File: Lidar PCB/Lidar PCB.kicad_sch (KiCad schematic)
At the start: 44 parts, among them J1 Barrel_Jack, J2 USB_C_Receptacle_USB2.0, J3 Conn_01x02_Socket, J4 Conn_01x06_Pin, J5 Conn_01x06_Socket, Q1 IRF740, SW1 SW_Push, U1 AMS1117-5.0, U2 ATmega328P-A, U3 FT232RL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

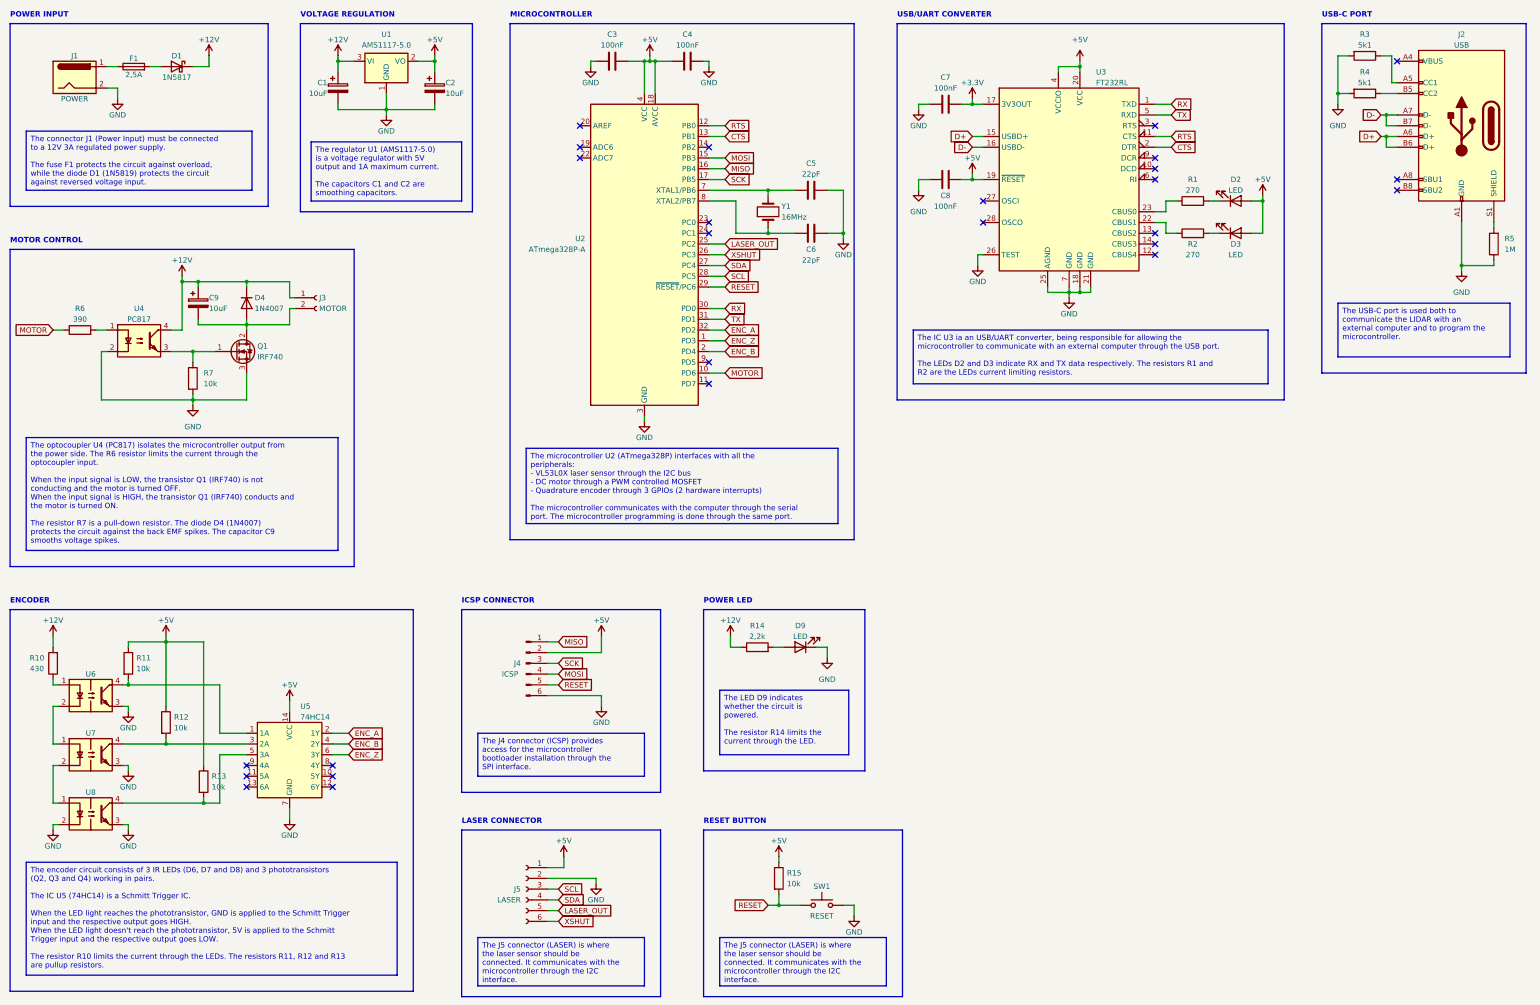
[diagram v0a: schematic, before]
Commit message: PCB input diode removed
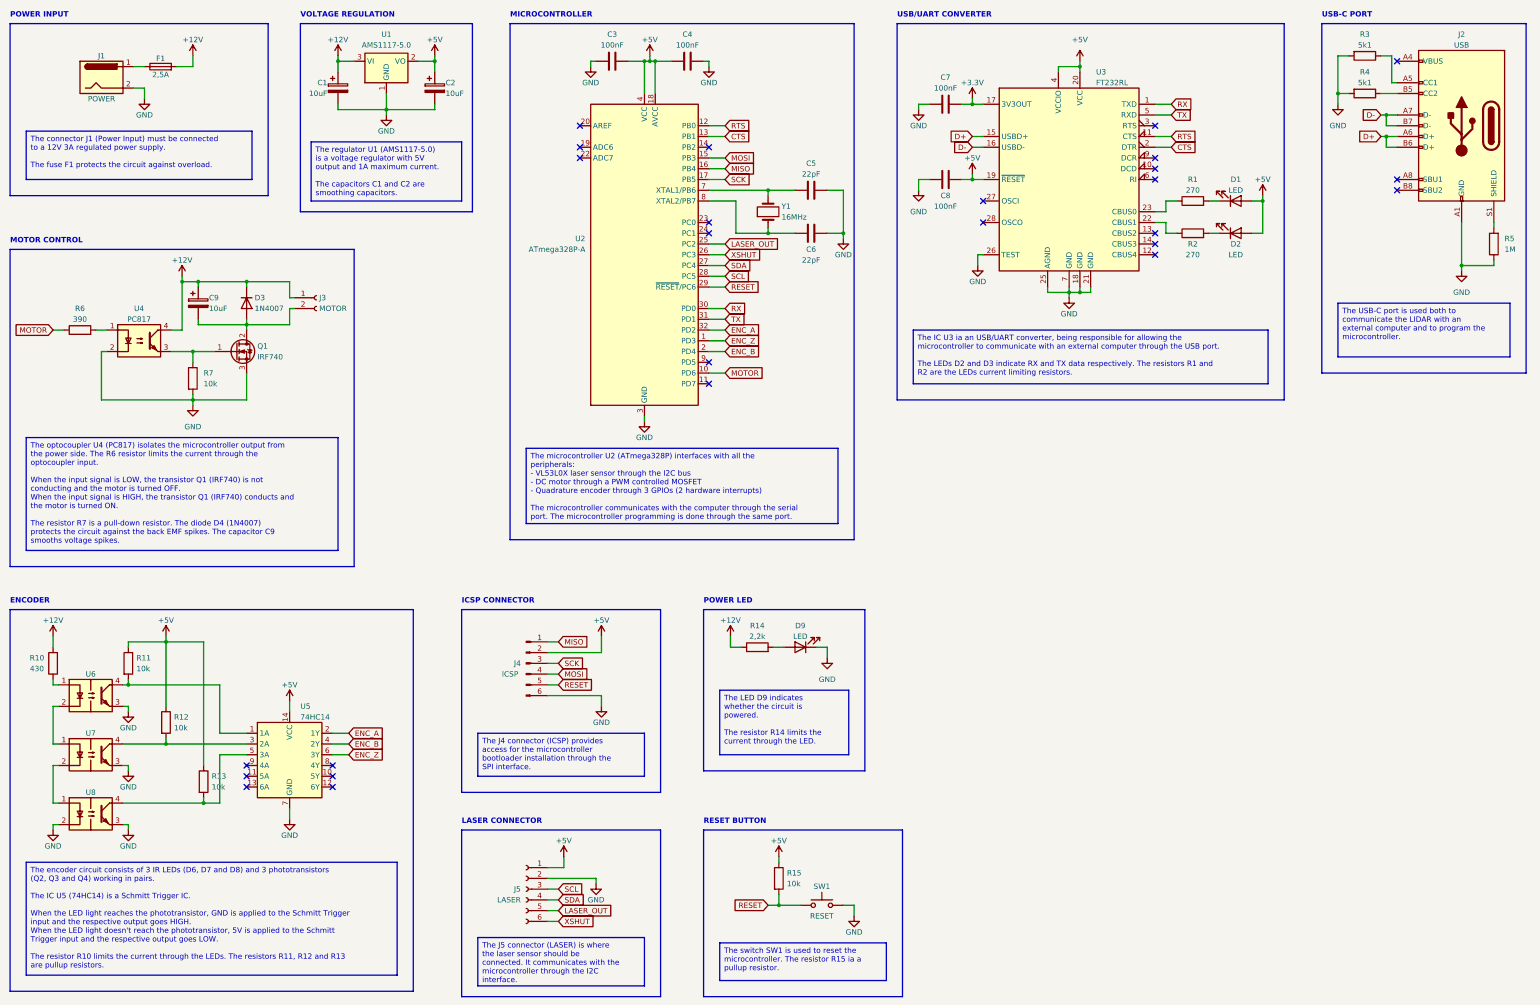
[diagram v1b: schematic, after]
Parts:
- removed D1: 1N5817, Diode_SMD:D_SMA, symbol Diode:1N5819
- renumbered D2 to D1, D3 to D2, D4 to D3
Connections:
- net +12V: now also F1.2
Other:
- moved on the sheet: F1, J1
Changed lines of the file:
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@@
     (stroke (width 0) (type default))
   )
-  (wire (pts (xy 72.39 41.91) (xy 76.2 41.91))
-    (stroke (width 0) (type default))
-  )
   (wire (pts (xy 78.74 204.47) (xy 85.09 204.47))
     (stroke (width 0) (type default))
@@
     (stroke (width 0) (type default))
   )
-  (wire (pts (xy 312.42 73.66) (xy 314.96 73.66))
-    (stroke (width 0) (type default))
-  )
   (wire (pts (xy 279.4 95.25) (xy 279.4 96.52))
     (stroke (width 0) (type default))
@@
     (stroke (width 0) (type default))
   )
-  (wire (pts (xy 76.2 41.91) (xy 76.2 39.37))
+  (wire (pts (xy 72.39 41.91) (xy 72.39 39.37))
     (stroke (width 0) (type default))
   )
@@
     (stroke (width 0) (type default))
   )
-  (wire (pts (xy 52.07 46.99) (xy 54.61 46.99))
+  (wire (pts (xy 58.42 46.99) (xy 60.96 46.99))
     (stroke (width 0) (type default))
   )
-  (wire (pts (xy 54.61 46.99) (xy 54.61 49.53))
+  (wire (pts (xy 60.96 46.99) (xy 60.96 49.53))
     (stroke (width 0) (type default))
   )
@@
     (stroke (width 0) (type default))
   )
+  (wire (pts (xy 312.42 73.66) (xy 314.96 73.66))
+    (stroke (width 0) (type default))
+  )
   (wire (pts (xy 353.06 39.37) (xy 355.6 39.37))
     (stroke (width 0) (type default))
@@
     (stroke (width 0) (type default))
   )
-  (wire (pts (xy 62.23 41.91) (xy 64.77 41.91))
+  (wire (pts (xy 68.58 41.91) (xy 72.39 41.91))
     (stroke (width 0) (type default))
   )
@@
     (stroke (width 0) (type default))
   )
-  (wire (pts (xy 52.07 41.91) (xy 54.61 41.91))
+  (wire (pts (xy 58.42 41.91) (xy 60.96 41.91))
     (stroke (width 0) (type default))
   )
@@
     (fill (type none))
   )
-  (rectangle (start 29.21 31.75) (end 90.17 74.93)
+  (rectangle (start 29.21 31.75) (end 90.17 72.39)
     (stroke (width 0) (type default))
     (fill (type none))
@@
     (effects (font (size 1.27 1.27)) (justify left top))
   )
-  (text_box "The connector J1 (Power Input) must be connected to a 12V 3A regulated power supply.\n\nThe fuse F1 protects the circuit against overload, while the diode D1 (1N5819) protects the circuit against reversed voltage input."
-    (at 33.02 57.15 0) (size 53.34 13.97)
+  (text_box "The connector J1 (Power Input) must be connected to a 12V 3A regulated power supply.\n\nThe fuse F1 protects the circuit against overload."
+    (at 33.02 57.15 0) (size 53.34 11.43)
     (stroke (width 0.3) (type default))
     (fill (type color) (color 194 194 194 1))
@@
     (effects (font (size 1.27 1.27)) (justify left top))
   )
-  (text_box "The J5 connector (LASER) is where the laser sensor should be connected. It communicates with the microcontroller through the I2C interface."
-    (at 196.85 247.65 0) (size 39.37 11.43)
+  (text_box "The switch SW1 is used to reset the microcontroller. The resistor R15 ia a pullup resistor."
+    (at 196.85 248.92 0) (size 39.37 8.89)
     (stroke (width 0.3) (type default))
     (fill (type color) (color 194 194 194 1))
@@
     )
   )
-  (symbol (lib_id "power:+12V") (at 76.2 39.37 0) (unit 1)
+  (symbol (lib_id "power:+12V") (at 72.39 39.37 0) (unit 1)
     (in_bom yes) (on_board yes) (dnp no)
-    (property "Reference" "#PWR02" (at 76.2 43.18 0)
+    (property "Reference" "#PWR02" (at 72.39 43.18 0)
       (effects (font (size 1.27 1.27)) hide)
     )
-    (property "Value" "+12V" (at 76.2 35.56 0)
+    (property "Value" "+12V" (at 72.39 35.56 0)
       (effects (font (size 1.27 1.27)))
     )
-    (property "Footprint" "" (at 76.2 39.37 0)
+    (property "Footprint" "" (at 72.39 39.37 0)
       (effects (font (size 1.27 1.27)) hide)
     )
-    (property "Datasheet" "" (at 76.2 39.37 0)
+    (property "Datasheet" "" (at 72.39 39.37 0)
       (effects (font (size 1.27 1.27)) hide)
     )
@@
     )
   )
-  (symbol (lib_id "power:GND") (at 54.61 49.53 0) (unit 1)
+  (symbol (lib_id "power:GND") (at 60.96 49.53 0) (unit 1)
     (in_bom yes) (on_board yes) (dnp no)
-    (property "Reference" "#PWR01" (at 54.61 55.88 0)
+    (property "Reference" "#PWR01" (at 60.96 55.88 0)
       (effects (font (size 1.27 1.27)) hide)
     )
-    (property "Value" "GND" (at 54.61 53.34 0)
+    (property "Value" "GND" (at 60.96 53.34 0)
       (effects (font (size 1.27 1.27)))
     )
-    (property "Footprint" "" (at 54.61 49.53 0)
+    (property "Footprint" "" (at 60.96 49.53 0)
       (effects (font (size 1.27 1.27)) hide)
     )
-    (property "Datasheet" "" (at 54.61 49.53 0)
+    (property "Datasheet" "" (at 60.96 49.53 0)
       (effects (font (size 1.27 1.27)) hide)
     )
@@
   (symbol (lib_id "Device:LED") (at 318.77 73.66 0) (mirror x) (unit 1)
     (in_bom yes) (on_board yes) (dnp no)
-    (property "Reference" "D2" (at 318.77 68.58 0)
+    (property "Reference" "D1" (at 318.77 68.58 0)
       (effects (font (size 1.27 1.27)))
     )
@@
       (project "Lidar PCB"
         (path "/bb86682b-faef-40ef-80b5-6cca2cd70904"
-          (reference "D2") (unit 1)
+          (reference "D1") (unit 1)
         )
       )
@@
   (symbol (lib_id "Diode:1N4007") (at 85.09 97.79 270) (unit 1)
     (in_bom yes) (on_board yes) (dnp no)
-    (property "Reference" "D4" (at 86.995 96.52 90)
+    (property "Reference" "D3" (at 86.995 96.52 90)
       (effects (font (size 1.27 1.27)) (justify left))
     )
@@
       (project "Lidar PCB"
         (path "/bb86682b-faef-40ef-80b5-6cca2cd70904"
-          (reference "D4") (unit 1)
+          (reference "D3") (unit 1)
         )
       )
     )
   )
-  (symbol (lib_id "Connector:Barrel_Jack") (at 44.45 44.45 0) (unit 1)
+  (symbol (lib_id "Connector:Barrel_Jack") (at 50.8 44.45 0) (unit 1)
     (in_bom yes) (on_board yes) (dnp no)
-    (property "Reference" "J1" (at 44.45 39.37 0)
+    (property "Reference" "J1" (at 50.8 39.37 0)
       (effects (font (size 1.27 1.27)))
     )
-    (property "Value" "Barrel_Jack" (at 44.45 39.37 0)
+    (property "Value" "Barrel_Jack" (at 50.8 39.37 0)
       (effects (font (size 1.27 1.27)) hide)
     )
-    (property "Footprint" "Connector_BarrelJack:BarrelJack_GCT_DCJ200-10-A_Horizontal" (at 45.72 45.466 0)
+    (property "Footprint" "Connector_BarrelJack:BarrelJack_GCT_DCJ200-10-A_Horizontal" (at 52.07 45.466 0)
       (effects (font (size 1.27 1.27)) hide)
     )
-    (property "Datasheet" "~" (at 45.72 45.466 0)
+    (property "Datasheet" "~" (at 52.07 45.466 0)
       (effects (font (size 1.27 1.27)) hide)
     )
-    (property "Description" "POWER" (at 44.45 49.53 0)
+    (property "Description" "POWER" (at 50.8 49.53 0)
       (effects (font (size 1.27 1.27)))
     )
@@
     )
   )
-  (symbol (lib_id "Device:Fuse") (at 58.42 41.91 90) (unit 1)
+  (symbol (lib_id "Device:Fuse") (at 64.77 41.91 90) (unit 1)
     (in_bom yes) (on_board yes) (dnp no)
-    (property "Reference" "F1" (at 58.42 40.005 90)
+    (property "Reference" "F1" (at 64.77 40.005 90)
       (effects (font (size 1.27 1.27)))
     )
-    (property "Value" "2,5A" (at 58.42 43.815 90)
+    (property "Value" "2,5A" (at 64.77 43.815 90)
       (effects (font (size 1.27 1.27)))
     )
-    (property "Footprint" "Fuse:Fuse_1206_3216Metric" (at 58.42 43.688 90)
+    (property "Footprint" "Fuse:Fuse_1206_3216Metric" (at 64.77 43.688 90)
       (effects (font (size 1.27 1.27)) hide)
     )
-    (property "Datasheet" "~" (at 58.42 41.91 0)
+    (property "Datasheet" "~" (at 64.77 41.91 0)
       (effects (font (size 1.27 1.27)) hide)
     )
@@
   (symbol (lib_id "Device:LED") (at 318.77 81.28 0) (mirror x) (unit 1)
     (in_bom yes) (on_board yes) (dnp no)
-    (property "Reference" "D3" (at 318.77 83.82 0)
+    (property "Reference" "D2" (at 318.77 83.82 0)
       (effects (font (size 1.27 1.27)))
     )
@@
       (project "Lidar PCB"
         (path "/bb86682b-faef-40ef-80b5-6cca2cd70904"
-          (reference "D3") (unit 1)
+          (reference "D2") (unit 1)
         )
       )
@@
         )
       )
-    )
-  )
-  (symbol (lib_id "Diode:1N5819") (at 68.58 41.91 0) (mirror y) (unit 1)
-    (in_bom yes) (on_board yes) (dnp no)
-    (property "Reference" "D1" (at 68.58 39.37 0)
-      (effects (font (size 1.27 1.27)))
-    )
-    (property "Value" "1N5817" (at 68.58 44.45 0)
-      (effects (font (size 1.27 1.27)))
-    )
-    (property "Footprint" "Diode_SMD:D_SMA" (at 68.58 46.355 0)
-      (effects (font (size 1.27 1.27)) hide)
-    )
-    (property "Datasheet" "http://www.vishay.com/docs/88525/1n5817.pdf" (at 68.58 41.91 0)
-      (effects (font (size 1.27 1.27)) hide)
-    )
-    (pin "1")
-    (pin "2")
-    (instances
-      (project "Lidar PCB"
-        (path "/bb86682b-faef-40ef-80b5-6cca2cd70904"
-          (reference "D1") (unit 1)
-        )
-      )
